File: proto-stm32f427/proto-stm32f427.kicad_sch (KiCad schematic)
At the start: 46 parts, among them J1 Conn_02x08_Odd_Even, J10 BOOT, J2 Conn_02x08_Odd_Even, J3 Conn_02x08_Odd_Even, J4 Conn_02x08_Odd_Even, J5 PWR_5v, J6 PWR_3v, J7 Conn_02x08_Odd_Even, J8 USB_C_Receptacle_USB2.0, J9 Conn_ARM_ETM_SWD_20, U1 NCV5501, U2 STM32F427VGTx, U3 W25Q32JVSS, Y1 8 MHz

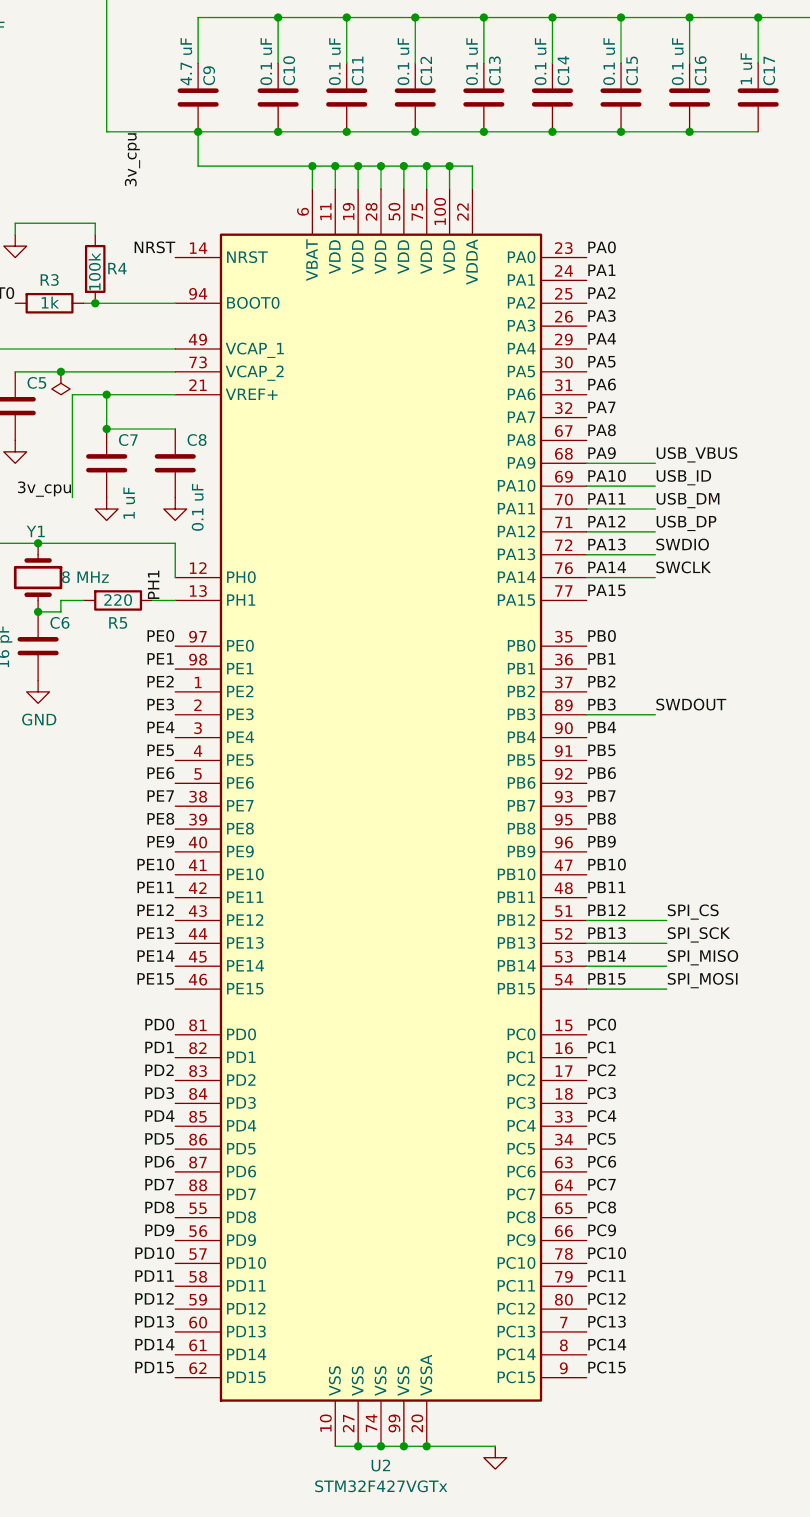
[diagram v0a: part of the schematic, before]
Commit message: Change out footprint for stm32h7 and rewire pins to accomodate
Same basic board, but now should mostly support the F7 and H7 series
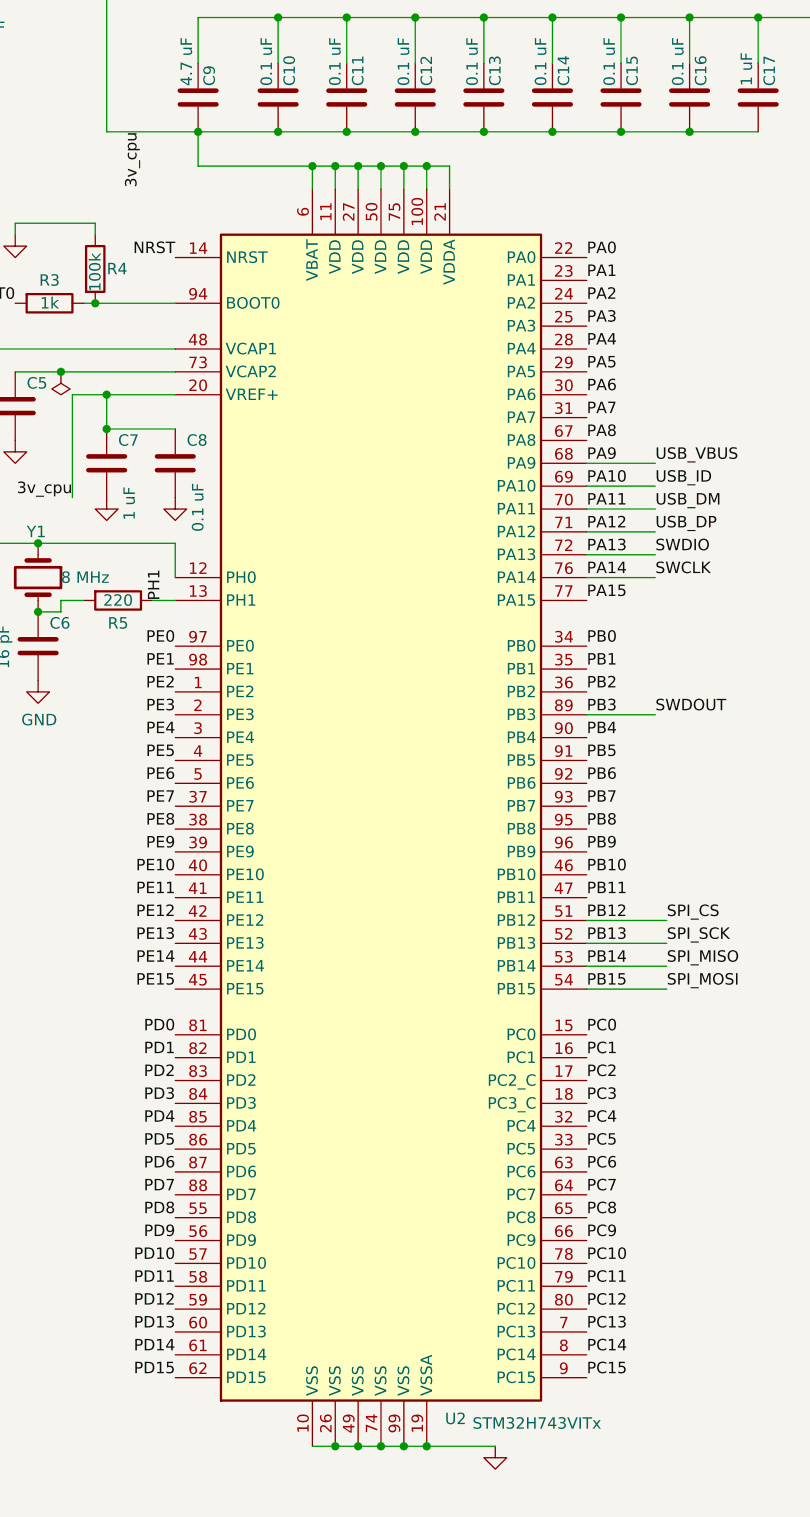
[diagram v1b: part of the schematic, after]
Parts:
- removed U2: STM32F427VGTx, Package_QFP:LQFP-100_14x14mm_P0.5mm, symbol MCU_ST_STM32F4:STM32F427VGTx
- added U2: STM32H743VITx, Package_QFP:LQFP-100_14x14mm_P0.5mm, symbol MCU_ST_STM32H7:STM32H743VITx
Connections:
- net 3v_cpu: now also U2.100 (VDD), U2.11 (VDD), U2.20 (VREF+), U2.21 (VDDA), U2.27 (VDD), U2.50 (VDD), U2.6 (VBAT), U2.75 (VDD)
- net GND: now also U2.10 (VSS), U2.19 (VSSA), U2.26 (VSS), U2.49 (VSS), U2.74 (VSS), U2.99 (VSS)
- net NRST: now also U2.14 (NRST)
- net PA0: now also U2.22 (PA0)
- net PA1: now also U2.23 (PA1)
- net PA10: now also U2.69 (PA10)
- net PA11: now also U2.70 (PA11)
- net PA12: now also U2.71 (PA12)
- net PA13: now also U2.72 (PA13)
- net PA14: now also U2.76 (PA14)
- net PA15: now also U2.77 (PA15)
- net PA2: now also U2.24 (PA2)
- net PA3: now also U2.25 (PA3)
- net PA4: now also U2.28 (PA4)
- net PA5: now also U2.29 (PA5)
- net PA6: now also U2.30 (PA6)
- net PA7: now also U2.31 (PA7)
- net PA8: now also U2.67 (PA8)
- net PA9: now also U2.68 (PA9)
- net PB0: now also U2.34 (PB0)
- net PB1: now also U2.35 (PB1)
- net PB10: now also U2.46 (PB10)
- net PB11: now also U2.47 (PB11)
- net PB12: now also U2.51 (PB12)
- net PB13: now also U2.52 (PB13)
- net PB14: now also U2.53 (PB14)
- net PB15: now also U2.54 (PB15)
- net PB2: now also U2.36 (PB2)
- net PB3: now also U2.89 (PB3)
- net PB4: now also U2.90 (PB4)
- net PB5: now also U2.91 (PB5)
- net PB6: now also U2.92 (PB6)
- net PB7: now also U2.93 (PB7)
- net PB8: now also U2.95 (PB8)
- net PB9: now also U2.96 (PB9)
- net PC0: now also U2.15 (PC0)
- net PC1: now also U2.16 (PC1)
- net PC10: now also U2.78 (PC10)
- net PC11: now also U2.79 (PC11)
- net PC12: now also U2.80 (PC12)
- net PC13: now also U2.7 (PC13)
- net PC14: now also U2.8 (PC14)
- net PC15: now also U2.9 (PC15)
- net PC2: now also U2.17 (PC2_C)
- net PC3: now also U2.18 (PC3_C)
- net PC4: now also U2.32 (PC4)
- net PC5: now also U2.33 (PC5)
- net PC6: now also U2.63 (PC6)
- net PC7: now also U2.64 (PC7)
- net PC8: now also U2.65 (PC8)
- net PC9: now also U2.66 (PC9)
- net PD0: now also U2.81 (PD0)
- net PD1: now also U2.82 (PD1)
- net PD10: now also U2.57 (PD10)
- net PD11: now also U2.58 (PD11)
- net PD12: now also U2.59 (PD12)
- net PD13: now also U2.60 (PD13)
- net PD14: now also U2.61 (PD14)
- net PD15: now also U2.62 (PD15)
- net PD2: now also U2.83 (PD2)
- net PD3: now also U2.84 (PD3)
- net PD4: now also U2.85 (PD4)
- net PD5: now also U2.86 (PD5)
- net PD6: now also U2.87 (PD6)
- net PD7: now also U2.88 (PD7)
- net PD8: now also U2.55 (PD8)
- net PD9: now also U2.56 (PD9)
- net PE0: now also U2.97 (PE0)
- net PE1: now also U2.98 (PE1)
- net PE10: now also U2.40 (PE10)
- net PE11: now also U2.41 (PE11)
- net PE12: now also U2.42 (PE12)
- net PE13: now also U2.43 (PE13)
- net PE14: now also U2.44 (PE14)
- net PE15: now also U2.45 (PE15)
- net PE2: now also U2.1 (PE2)
- net PE3: now also U2.2 (PE3)
- net PE4: now also U2.3 (PE4)
- net PE5: now also U2.4 (PE5)
- net PE6: now also U2.5 (PE6)
- net PE7: now also U2.37 (PE7)
- net PE8: now also U2.38 (PE8)
- net PE9: now also U2.39 (PE9)
- net PH0: now also U2.12 (PH0)
- net PH1: now also U2.13 (PH1)
- net at C3.1: now also U2.48 (VCAP1)
- net at C5.1: now also U2.73 (VCAP2)
- net at R3.1, R4.2: now also U2.94 (BOOT0)
